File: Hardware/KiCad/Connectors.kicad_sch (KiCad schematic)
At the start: 51 parts

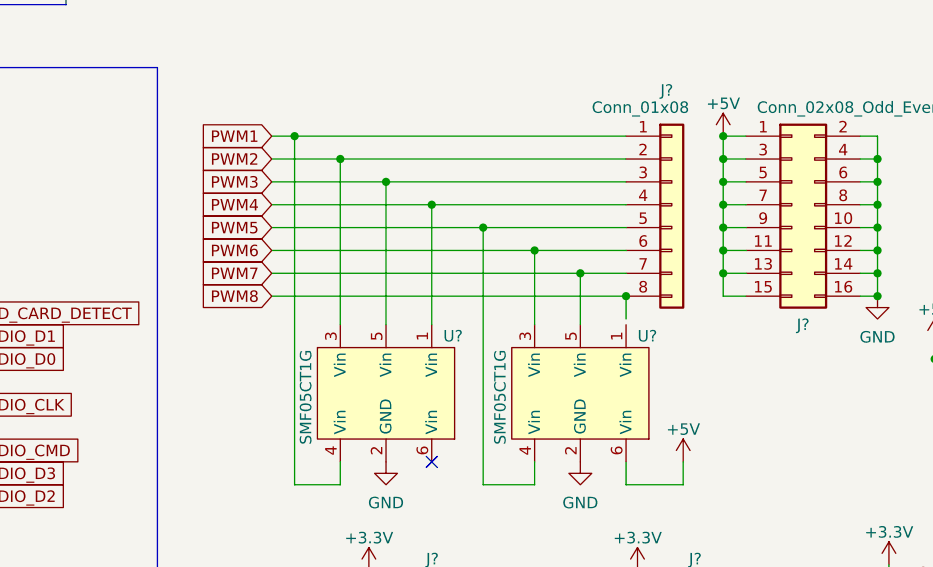
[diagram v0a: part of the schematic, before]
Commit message: Changed max PPM ESC controlers from 8->6 to make room for a buzzer and IBUS connection
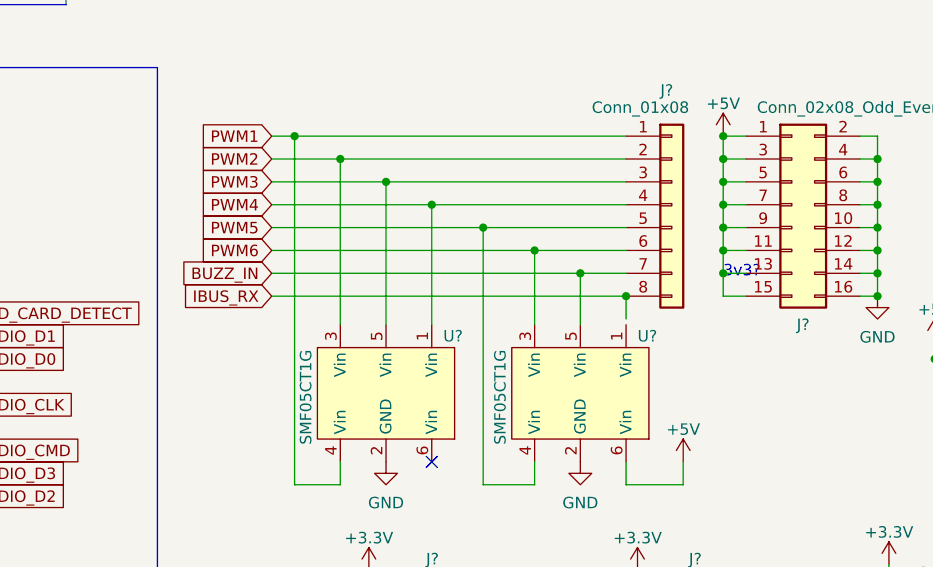
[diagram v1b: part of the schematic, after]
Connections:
- net PWM7 renamed BUZZ_IN
- net PWM8 renamed IBUS_RX
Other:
- note added: "3v3?"
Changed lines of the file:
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@@
+    (effects (font (size 1.27 1.27)) (justify left bottom))
+  )
+  (text "3v3?" (at 231.14 107.95 0)
     (effects (font (size 1.27 1.27)) (justify left bottom))
   )
@@
     )
   )
+  (global_label "IBUS_RX" (shape input) (at 180.975 109.855 180) (fields_autoplaced)
+    (effects (font (size 1.27 1.27)) (justify right))
+    (property "Intersheet References" "${INTERSHEET_REFS}" (id 0) (at 170.7 109.7756 0)
+      (effects (font (size 1.27 1.27)) (justify right) hide)
+    )
+  )
+  (global_label "BUZZ_IN" (shape input) (at 180.975 107.315 180) (fields_autoplaced)
+    (effects (font (size 1.27 1.27)) (justify right))
+    (property "Intersheet References" "${INTERSHEET_REFS}" (id 0) (at 170.6395 107.2356 0)
+      (effects (font (size 1.27 1.27)) (justify right) hide)
+    )
+  )
   (global_label "REG_IN" (shape input) (at 118.11 23.495 0) (fields_autoplaced)
     (effects (font (size 1.27 1.27)) (justify left))
@@
     )
   )
-  (global_label "PWM8" (shape input) (at 180.975 109.855 180) (fields_autoplaced)
-    (effects (font (size 1.27 1.27)) (justify right))
-    (property "Intersheet References" "${INTERSHEET_REFS}" (id 0) (at 173.1795 109.7756 0)
-      (effects (font (size 1.27 1.27)) (justify right) hide)
-    )
-  )
   (global_label "SDIO_CMD" (shape input) (at 147.955 127 0) (fields_autoplaced)
     (effects (font (size 1.27 1.27)) (justify left))
@@
       (effects (font (size 1.27 1.27)) (justify right) hide)
     )
-  )
-  (global_label "PWM7" (shape input) (at 180.975 107.315 180) (fields_autoplaced)
-    (effects (font (size 1.27 1.27)) (justify right))
-    (property "Intersheet References" "${INTERSHEET_REFS}" (id 0) (at 173.1795 107.2356 0)
-      (effects (font (size 1.27 1.27)) (justify right) hide)
-    )

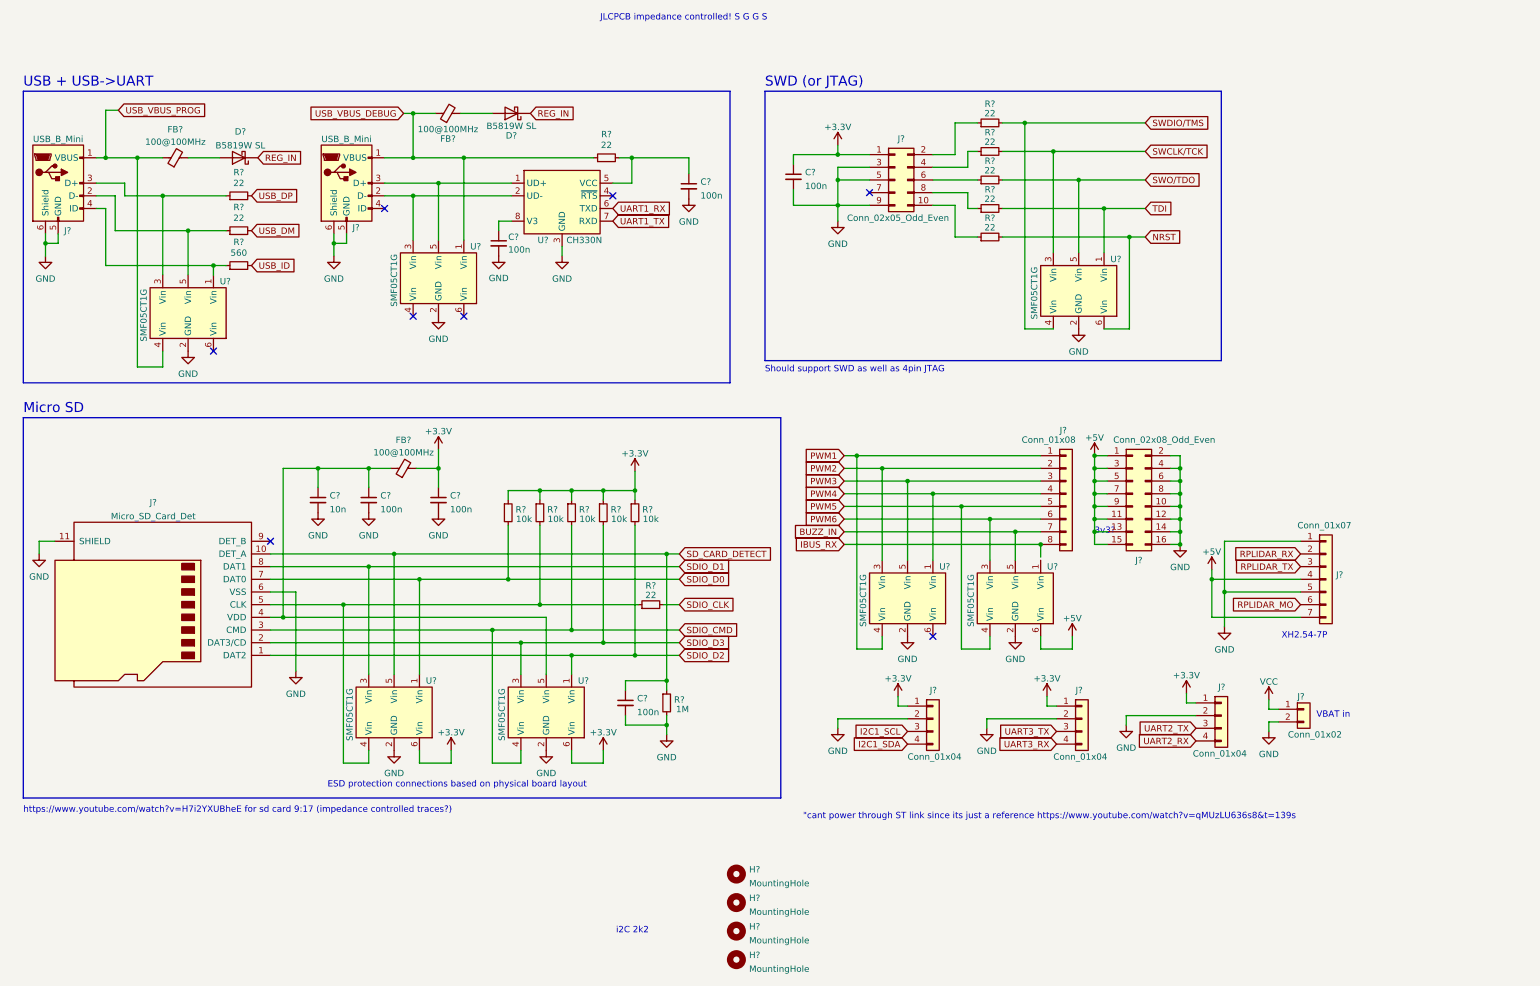
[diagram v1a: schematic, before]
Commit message: Added pinlables, added SD cardholder footprint, fixed VBUS connection, added termination resistors for high frequency signals, improved schematic layout
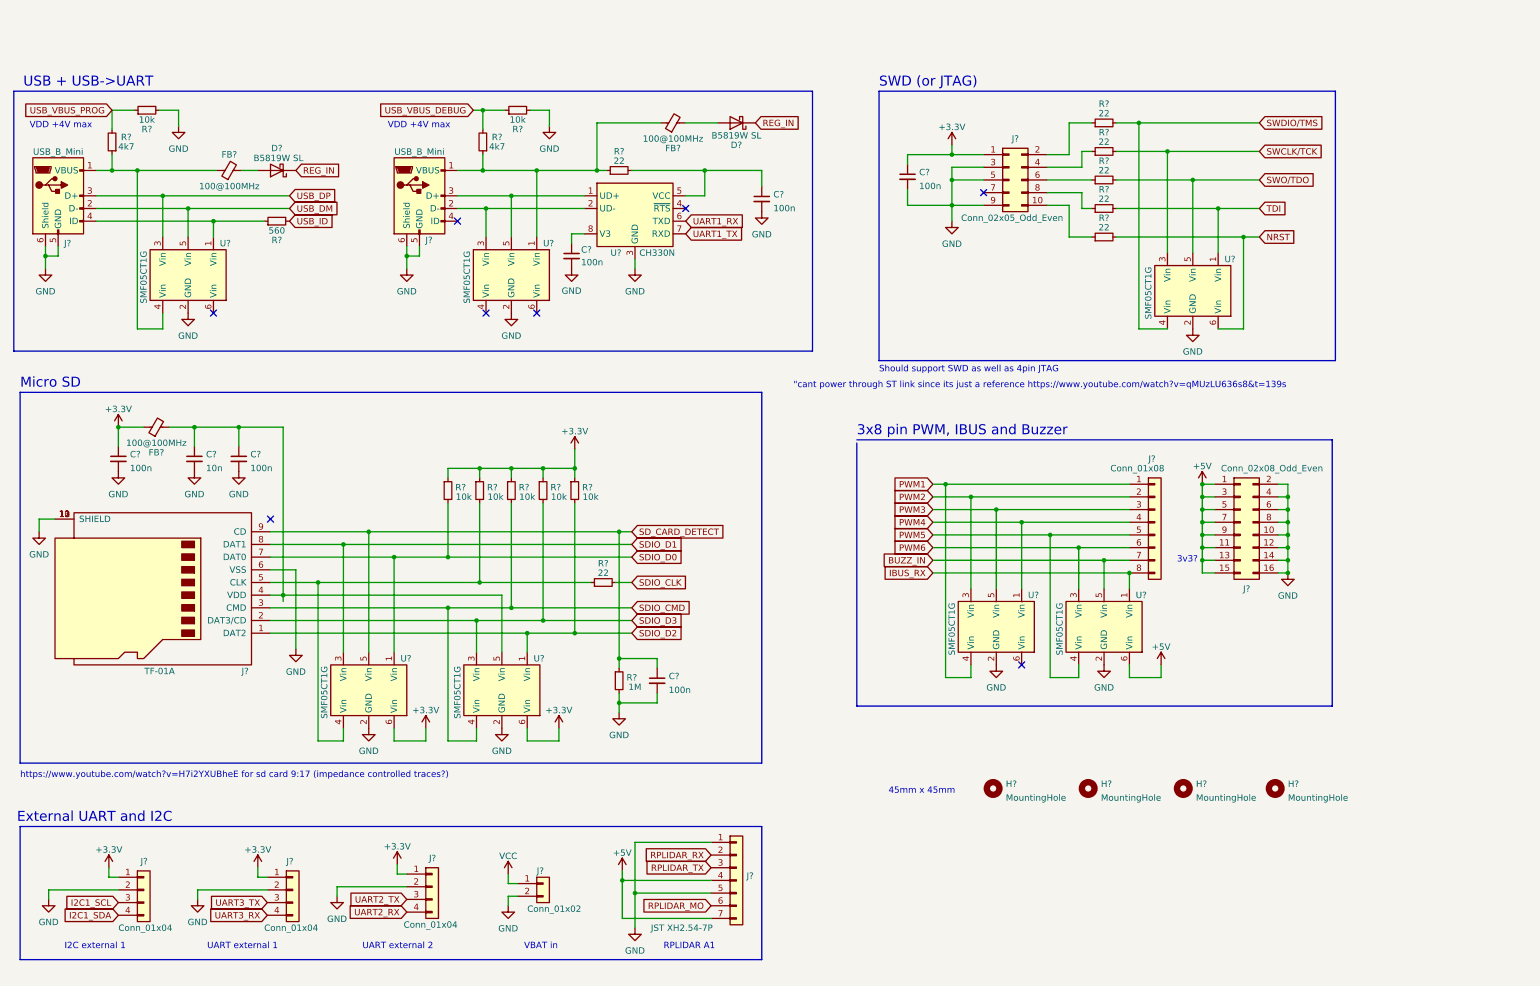
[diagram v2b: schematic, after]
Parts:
- removed FB?: 100@100MHz, symbol Device:FerriteBead_Small
- removed J?: Micro_SD_Card_Det, symbol Connector:Micro_SD_Card_Det
- removed R? (x2): 22, symbol Device:R_Small
- added FB?: 100@100MHz, symbol Device:FerriteBead_Small
- added J?: TF-01A, flightController:TF-01A, symbol flightController:Micro_SD_Card
- added R? (x2): 4k7, symbol Device:R_Small
- added R? (x2): 10k, symbol Device:R_Small
- J?: value Conn_01x07 -> JST XH2.54-7P
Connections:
- net +3V3: now also FB?.1
- net GND: now also J?.10 (SHIELD), J?.11 (SHIELD), J?.12 (SHIELD), J?.13 (SHIELD), J?.6 (VSS), R?.2, R?.2
- net IBUS_RX: now also U?.1 (Vin)
- net SDIO_CMD: now also J?.3 (CMD)
- net SDIO_D0: now also J?.7 (DAT0)
- net SDIO_D1: now also J?.8 (DAT1)
- net SDIO_D2: now also J?.1 (DAT2)
- net SDIO_D3: now also J?.2 (DAT3/CD)
- net SD_CARD_DETECT: now also J?.9 (CD)
- net USB_DM: now also J?.2 (D-), U?.5 (Vin)
- net USB_DP: now also J?.3 (D+), U?.3 (Vin)
- net USB_VBUS_DEBUG: now also R?.1, R?.2; no longer FB?.1, J?.1 (VBUS), R?.1, U?.1 (Vin)
- net USB_VBUS_PROG: now also R?.1, R?.2; no longer FB?.1, J?.1 (VBUS), U?.4 (Vin)
- net at R?.1, R?.2, U?.4 (Vin): now also J?.5 (CLK)
- net at C?.1, C?.1, U?.5 (Vin): now also FB?.2, J?.4 (VDD)
- new net: FB?.1, J?.1 (VBUS), R?.1, R?.1, U?.1 (Vin)
- new net: FB?.1, J?.1 (VBUS), R?.1, U?.4 (Vin)
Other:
- note added: "3x8 pin PWM, IBUS and Buzzer"
- note added: "45mm x 45mm"
- note added: "External UART and I2C"
- note added: "I2C external 1"
- note added: "RPLIDAR A1"
- note added: "UART external 1"
- note added: "UART external 2"
- note added: "VDD +4V max"
- note removed: "ESD protection connections based on physical board layout"
- note removed: "JLCPCB impedance controlled! S G G S"
- note removed: "XH2.54-7P"
- note removed: "i2C 2k2"
- moved on the sheet: C?, D?, FB?, H?, J?, R?, U?

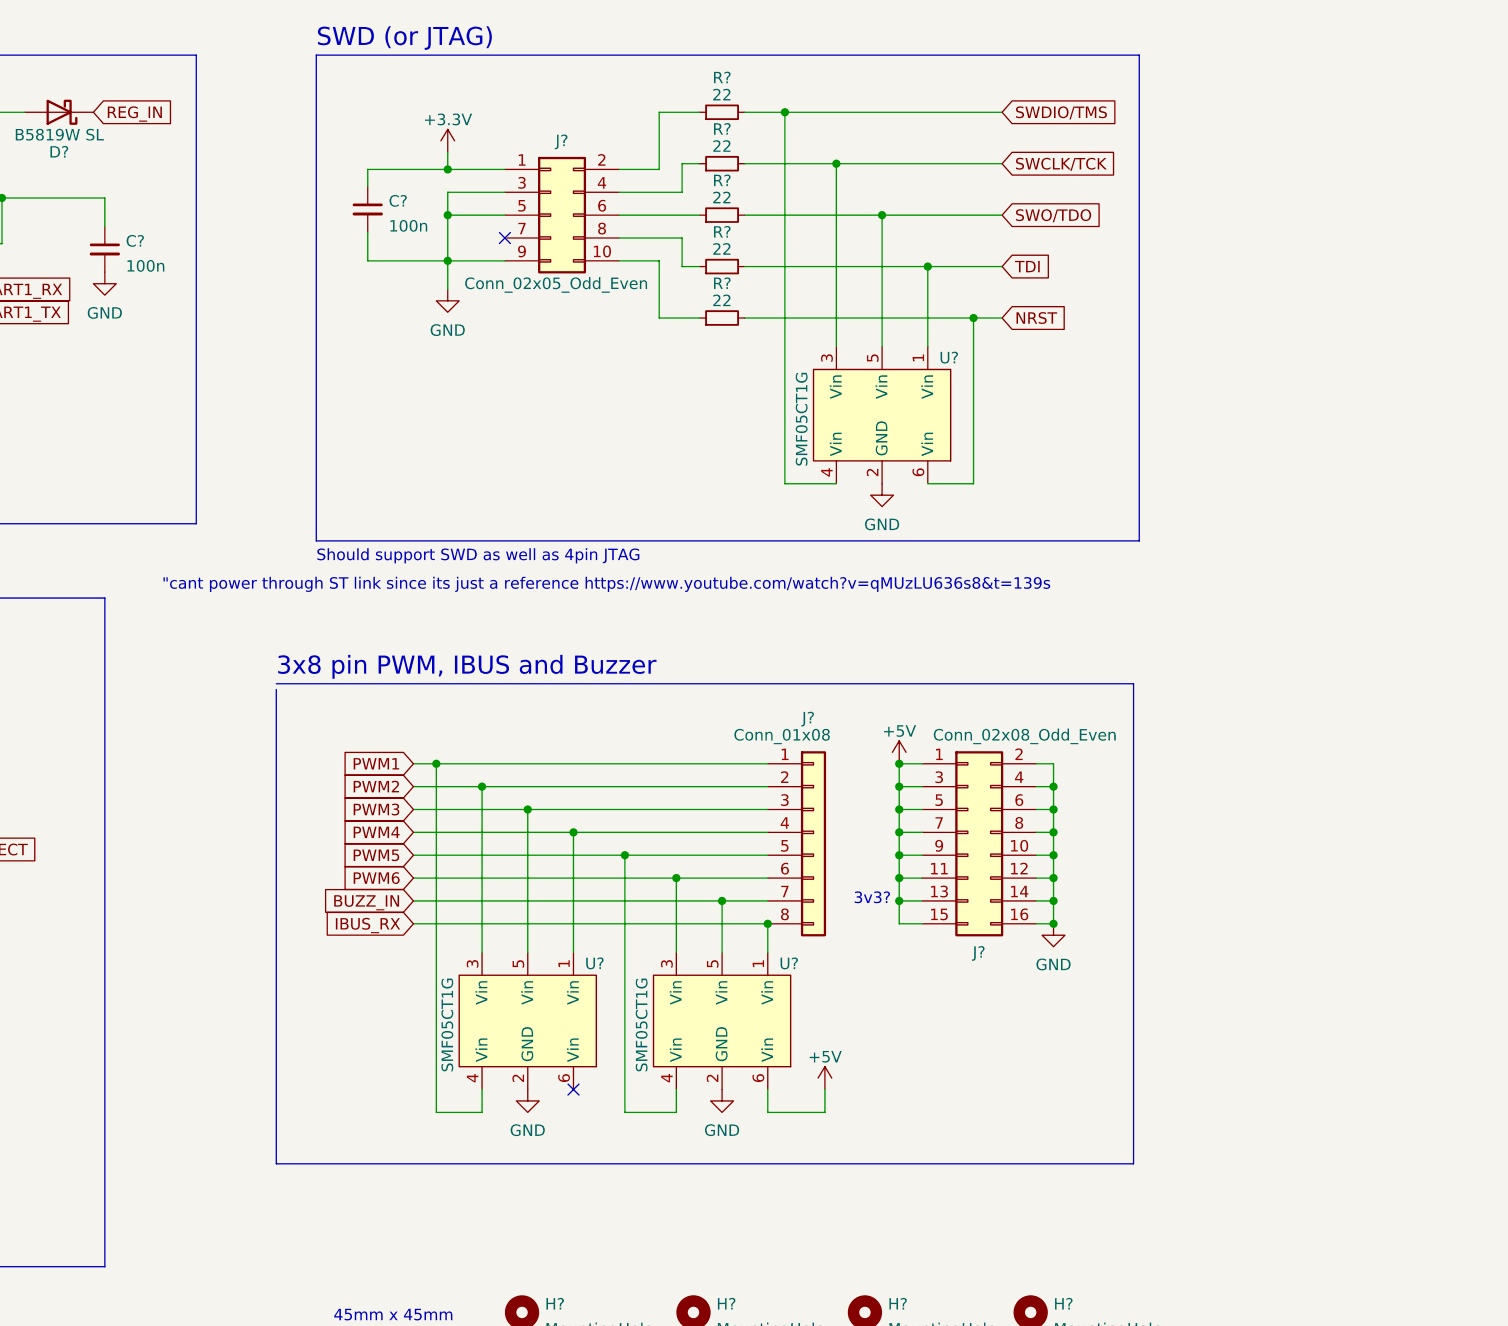
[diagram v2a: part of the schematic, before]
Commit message: More pin definitions
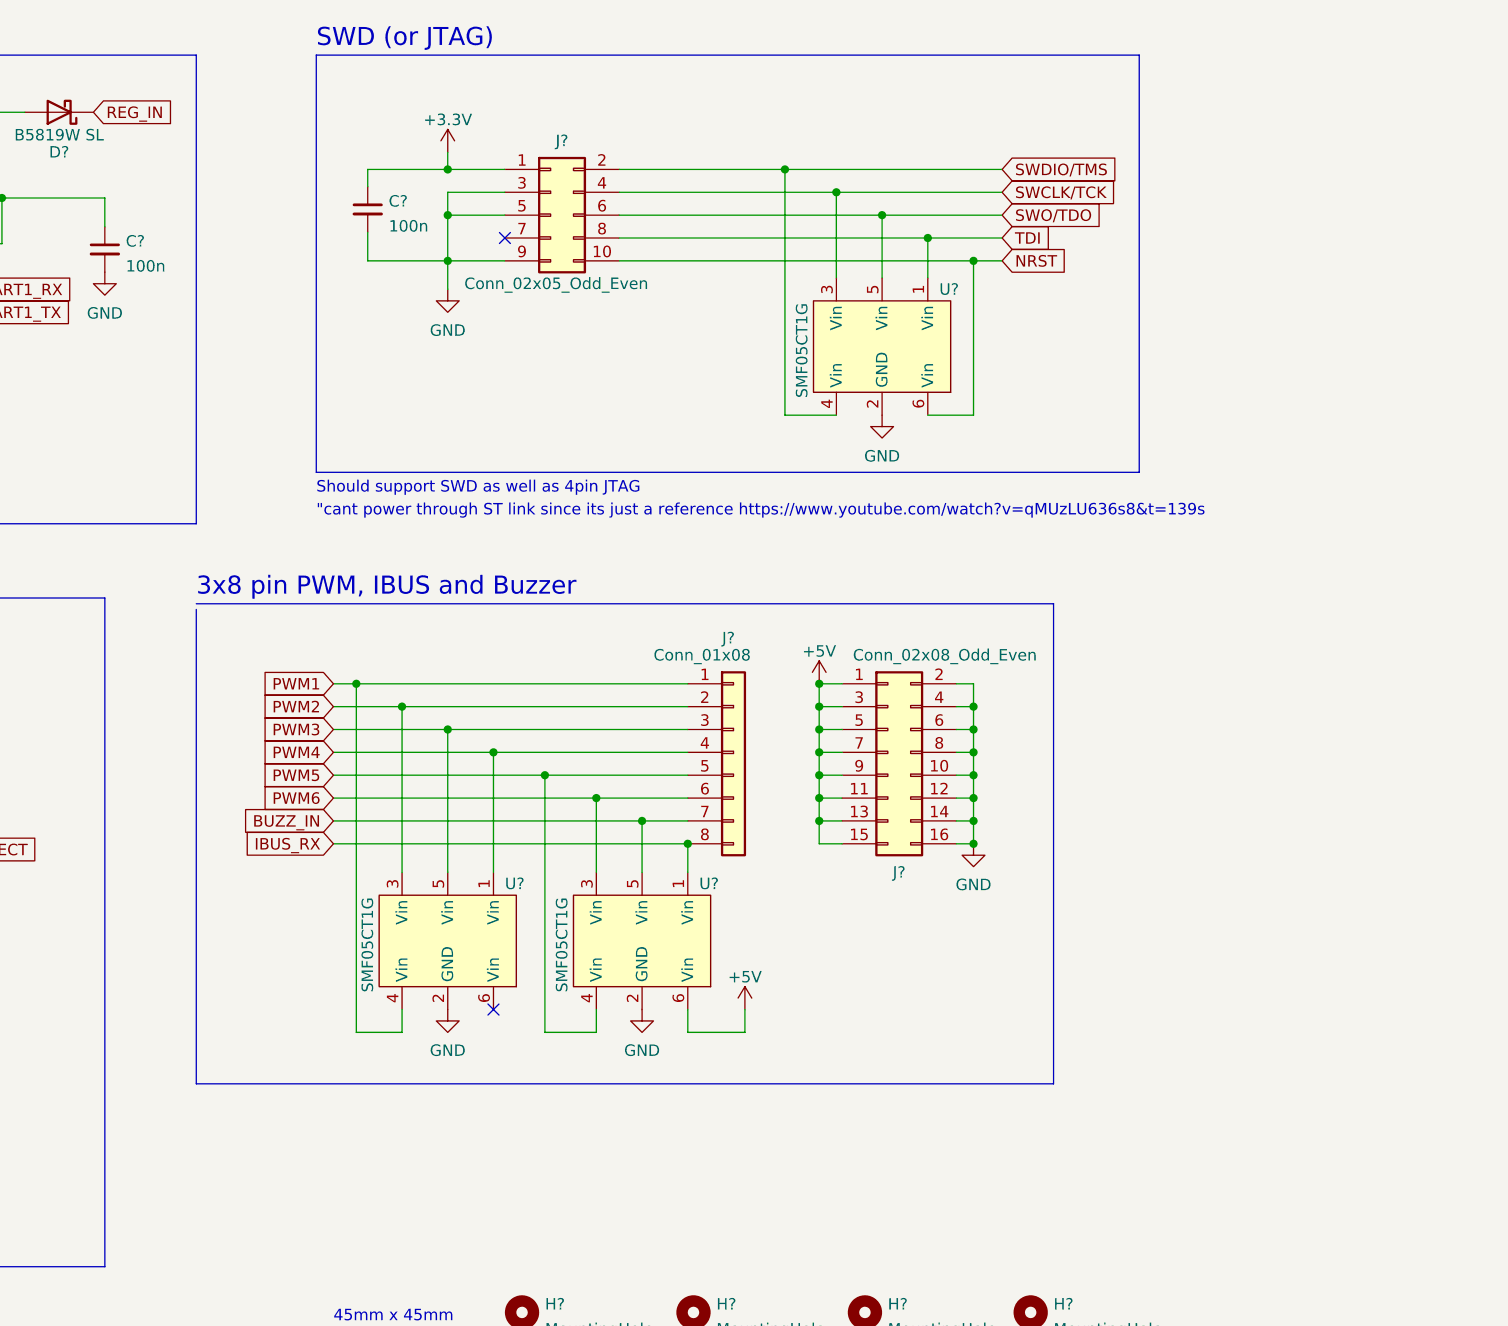
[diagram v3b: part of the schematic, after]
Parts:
- removed R? (x5): 22, symbol Device:R_Small
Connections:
- net NRST: now also J?.10 (Pin_10)
- net SWCLK/TCK: now also J?.4 (Pin_4)
- net SWDIO/TMS: now also J?.2 (Pin_2)
- net SWO/TDO: now also J?.6 (Pin_6)
- net TDI: now also J?.8 (Pin_8)
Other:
- note removed: "3v3?"
- moved on the sheet: J?, U?
